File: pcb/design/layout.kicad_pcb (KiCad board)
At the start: 2 copper layers, 55.6 x 83.8 mm, 7 parts

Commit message: fix pcb design
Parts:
- removed the G*** at (0.00, 0.00) (x7)
- added G*** (x7): LOGO, LOGO, F.Cu at (0.00, 0.00)

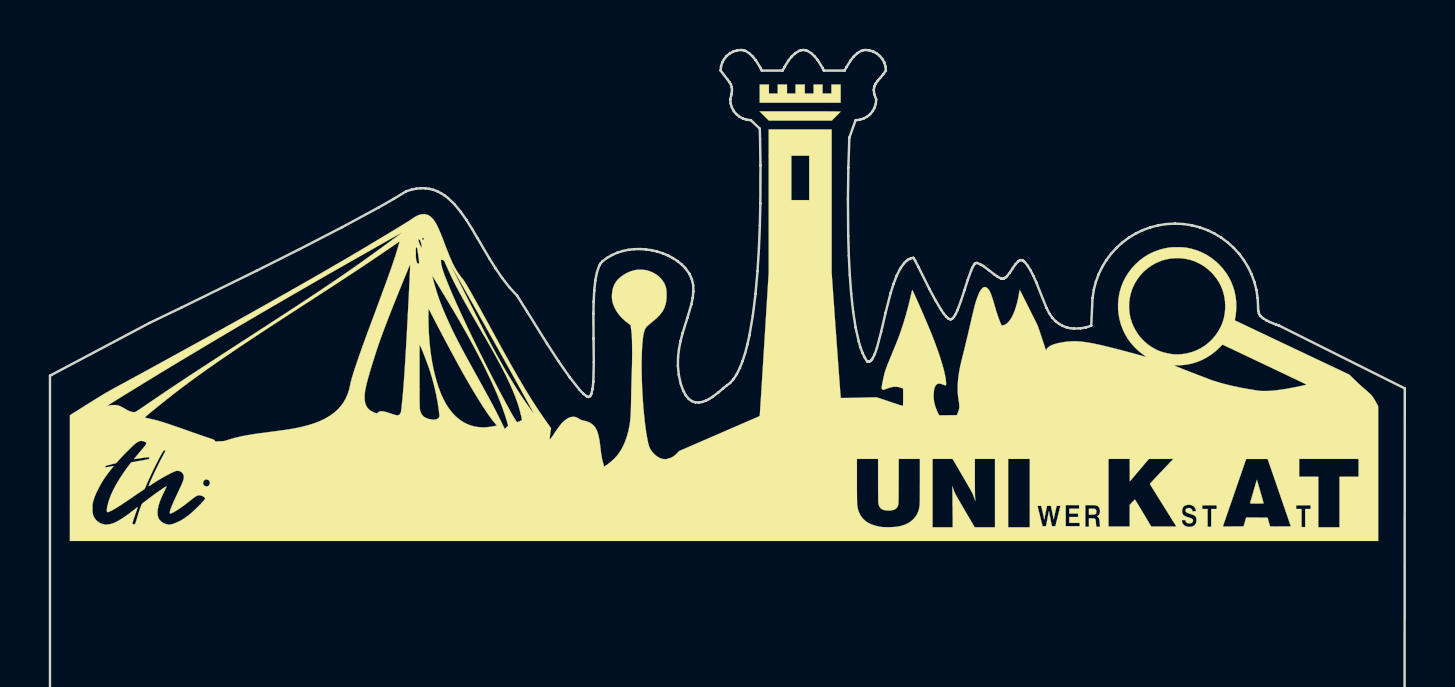
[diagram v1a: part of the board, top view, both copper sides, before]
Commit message: attempt to compensate for printing errors in silk screen
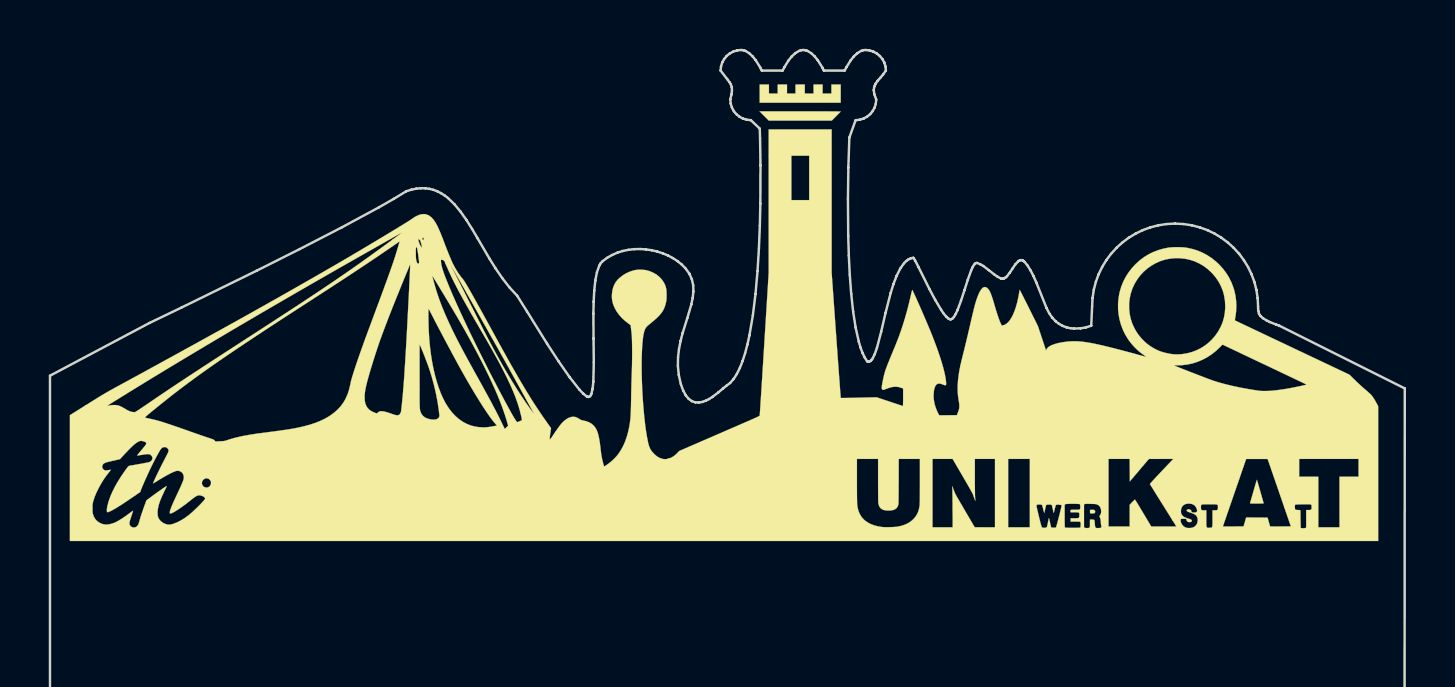
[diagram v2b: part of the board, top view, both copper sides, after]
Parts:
- removed the G*** at (0.00, 0.00) (x7)
- added G*** (x7): LOGO, LOGO, F.Cu at (0.00, 0.00)
